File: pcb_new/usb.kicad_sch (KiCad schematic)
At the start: 28 parts, among them J14 68021-204HLF, J7 632723300011, U10 TPS2021D, U2 CAHCT1G14QDBVRQ1, U6 USB3340-EZK-TR

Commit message: initial test of new board
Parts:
- R36: Arrow ID CPF0402B8K06E1 -> (none); Description_1 CPF 0402 8K06 0.1% 25PPM 1K RL -> Thin Film Resistors - SMD 0402 8.06Kohm .1% AEC-Q200; DigiKey ID A103004CT-ND -> (none); Mfr. Name TE Connectivity -> Panasonic; Mfr. Number CPF0402B8K06E1 -> ERA-2AEB8061X; Mouser ID 279-CPF0402B8K06E1 -> 667-ERA-2AEB8061X; Mouser URL https://www.mouser.de/ProductDetail/TE-Connectivity-Holswor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 -> https://www.mouser.de/ProductDetail/Panasonic/ERA-2AEB8061X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
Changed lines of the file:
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@@
 			)
 		)
-		(property "Datasheet" "https://www.mouser.de/datasheet/2/418/8/ENG_DS_1773200_N2-1954016.pdf"
+		(property "Datasheet" "https://industrial.panasonic.com/cdbs/www-data/pdf/RDM0000/AOA0000C307.pdf"
 			(at 110.49 130.81 0)
 			(effects
@@
 			)
 		)
-		(property "Description" "CPF 0402 8K06 0.1% 25PPM 1K RL"
+		(property "Description" "Thin Film Resistors - SMD 0402 8.06Kohm .1% AEC-Q200"
 			(at 110.49 130.81 0)
 			(effects
@@
 			)
 		)
-		(property "Mouser URL" "https://www.mouser.de/ProductDetail/TE-Connectivity-Holsworthy/CPF0402B8K06E1?qs=iJVBkmKXgrk320lBsnTGsA%3D%3D&utm_source=octopart&utm_medium=aggregator&utm_campaign=279-CPF0402B8K06E1&utm_content=TE+Connectivity"
+		(property "Mouser URL" "https://www.mouser.de/ProductDetail/Panasonic/ERA-2AEB8061X?qs=nuXzIS8loXGZUdwZTdWhRQ%3D%3D"
 			(at 110.49 133.81 0)
 			(effects
@@
 			)
 		)
-		(property "Mfr. Name" "TE Connectivity"
+		(property "Mfr. Name" "Panasonic"
 			(at 110.49 133.81 0)
 			(effects
@@
 			)
 		)
-		(property "Mfr. Number" "CPF0402B8K06E1"
+		(property "Mfr. Number" "ERA-2AEB8061X"
 			(at 110.49 133.81 0)
 			(effects
@@
 			)
 		)
-		(property "DigiKey ID" "A103004CT-ND"
+		(property "DigiKey ID" ""
 			(at 110.49 133.81 0)
 			(effects
@@
 			)
 		)
-		(property "Mouser ID" "279-CPF0402B8K06E1"
+		(property "Mouser ID" "667-ERA-2AEB8061X"
 			(at 110.49 133.81 0)
 			(effects
@@
 			)
 		)
-		(property "Description_1" "CPF 0402 8K06 0.1% 25PPM 1K RL"
+		(property "Description_1" "Thin Film Resistors - SMD 0402 8.06Kohm .1% AEC-Q200"
 			(at 110.49 133.81 0)
 			(effects
@@
 			)
 		)
-		(property "Arrow ID" "CPF0402B8K06E1"
+		(property "Arrow ID" ""
 			(at 110.49 133.81 0)
 			(effects

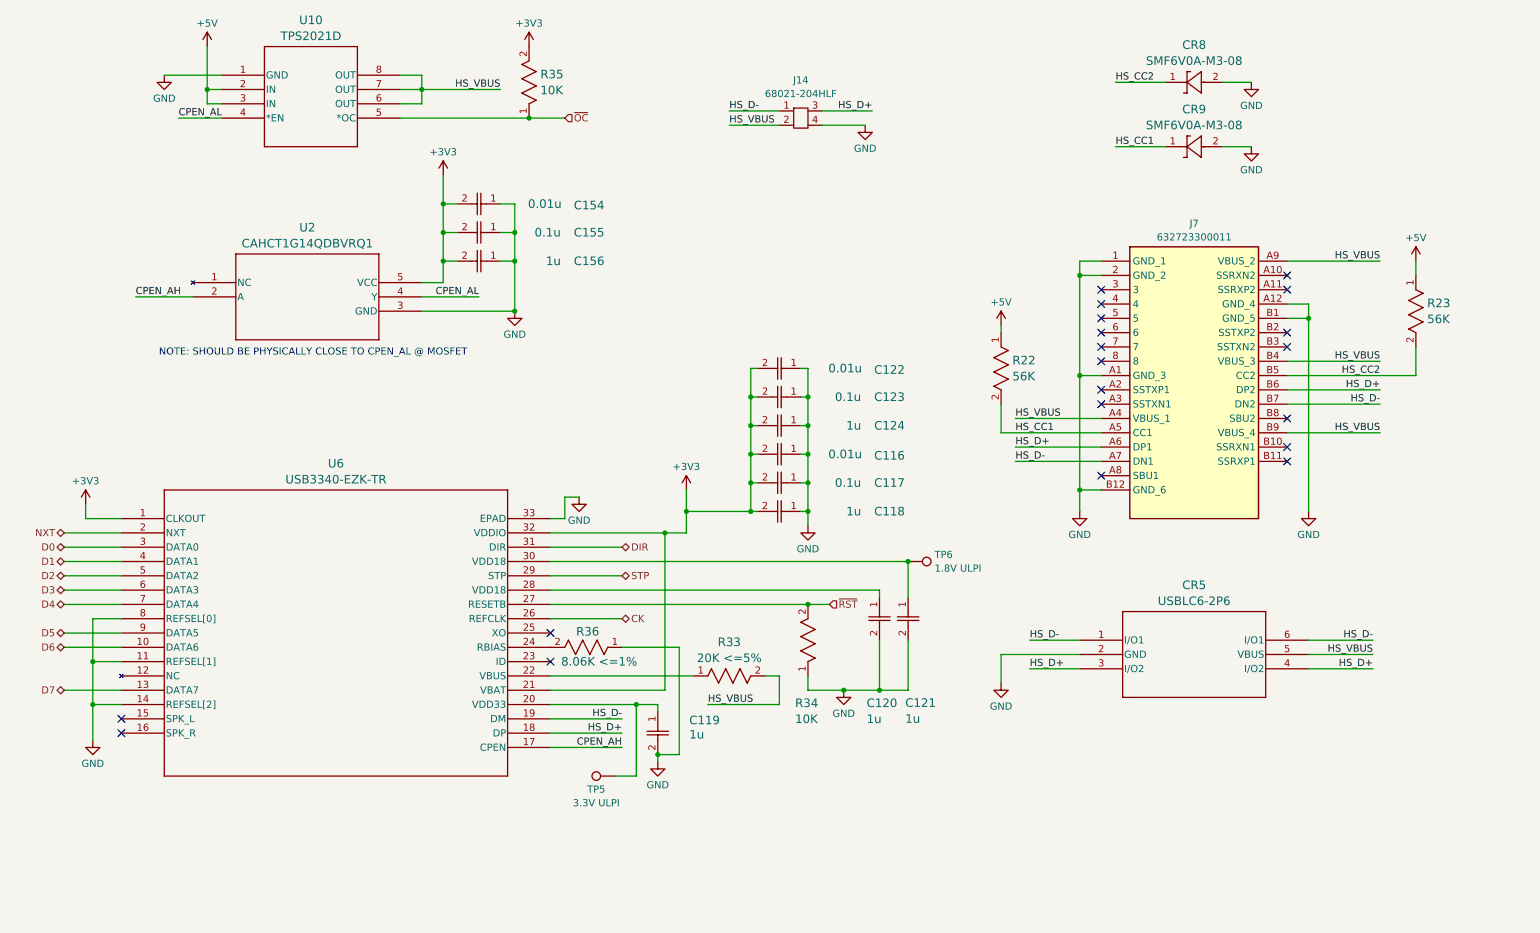
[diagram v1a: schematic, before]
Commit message: fix ULPI PHY wiring (ref #62)
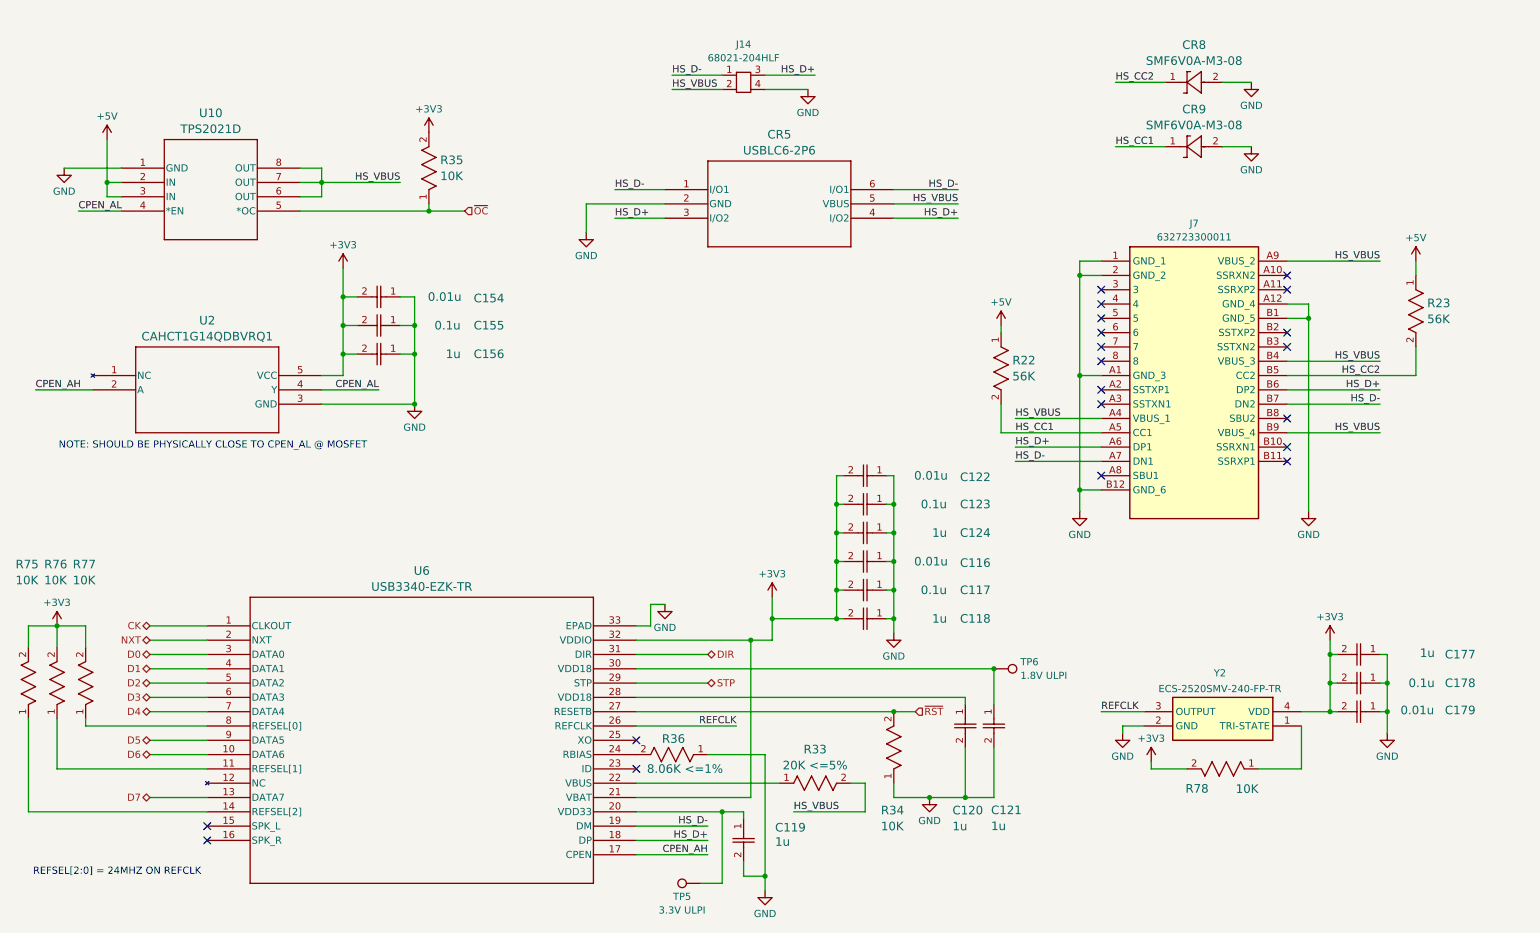
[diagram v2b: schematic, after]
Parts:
- added C177: 1u, OroLink:cap_UMK105 CG080CV-F_TAY, symbol OroLink:JMK105BJ105KVHF
- added C178: 0.1u, OroLink:CAP_MSAS1L-3_TAY, symbol OroLink:MSAST1L3YB5104KFNA01
- added C179: 0.01u, OroLink:CAP_0402_N_WAL, symbol OroLink:0402B103J160CT
- added R75, R76, R77, R78: 10K, OroLink:STA_RMCF0402_STP, symbol OroLink:RMCF0402FT10K0
- added Y2: ECS-2520SMV-240-FP-TR, ECS2520SMV240FPTR, symbol OroLink:ECS-2520SMV-240-FP-TR
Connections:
- net +3V3: now also C177.2, C178.2, C179.2, R75.2, R76.2, R77.2, R78.2, Y2.4 (VDD); no longer U6.1 (CLKOUT)
- net CK: now also U6.1 (CLKOUT); no longer U6.26 (REFCLK)
- net GND: now also C177.1, C178.1, C179.1, Y2.2 (GND); no longer U6.11 (REFSEL[1]), U6.14 (REFSEL[2]), U6.8 (REFSEL[0])
- new net: R76.1, U6.11 (REFSEL[1])
- new net: R75.1, U6.14 (REFSEL[2])
- new net: R77.1, U6.8 (REFSEL[0])
- new net: R78.1, Y2.1 (TRI-STATE)
- new net REFCLK: U6.26 (REFCLK), Y2.3 (OUTPUT)
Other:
- note added: "REFSEL[2:0] = 24MHZ ON REFCLK"
- moved on the sheet: C116, C117, C118, C119, C120, C121, C122, C123, C124, C154, C155, C156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

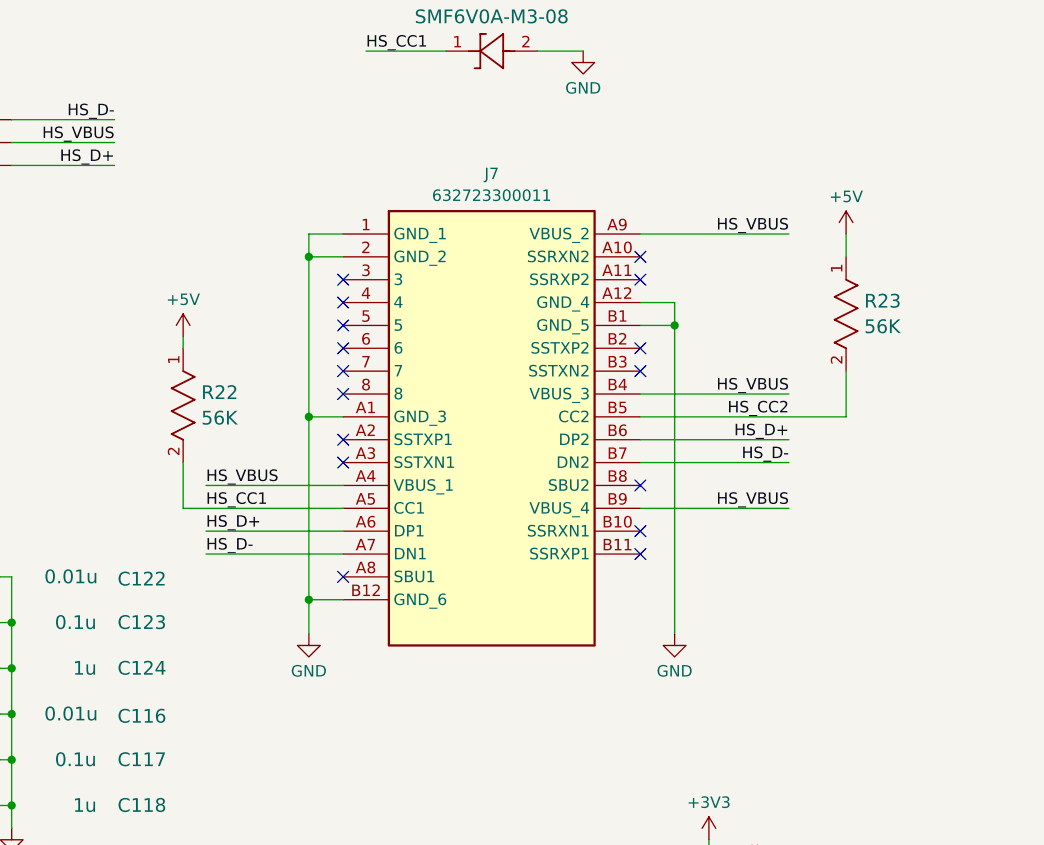
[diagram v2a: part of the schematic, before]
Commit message: replace USB-C receptacle (ref #73)
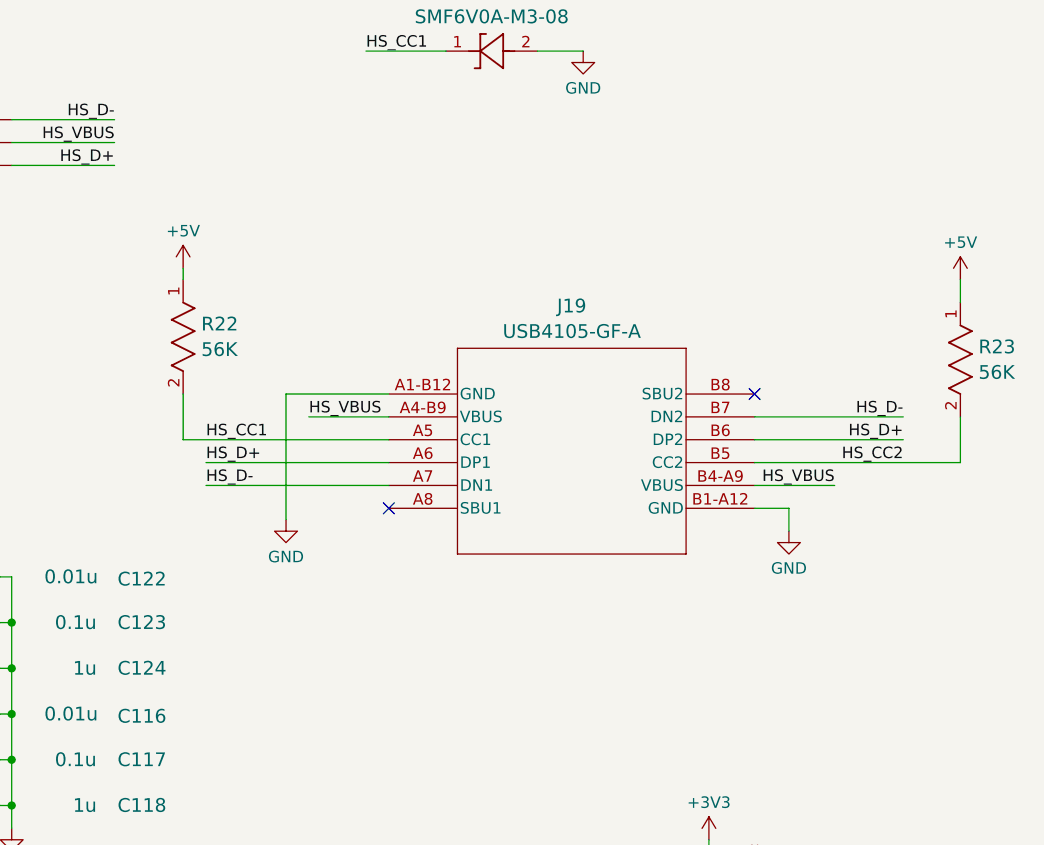
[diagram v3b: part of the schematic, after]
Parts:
- removed J7: 632723300011, OroLink:632723300011, symbol OroLink:632723300011
- added J19: USB4105-GF-A, OroLink:USB4105_GCT, symbol OroLink:USB4105-GF-A
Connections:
- net GND: now also J19.A1-B12 (GND), J19.B1-A12 (GND)
- net HS_CC1: now also J19.A5 (CC1)
- net HS_CC2: now also J19.B5 (CC2)
- net HS_D+: now also J19.A6 (DP1), J19.B6 (DP2)
- net HS_D-: now also J19.A7 (DN1), J19.B7 (DN2)
- net HS_VBUS: now also J19.A4-B9 (VBUS), J19.B4-A9 (VBUS)
- no-connect marks 20 -> 6
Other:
- moved on the sheet: R22, R23

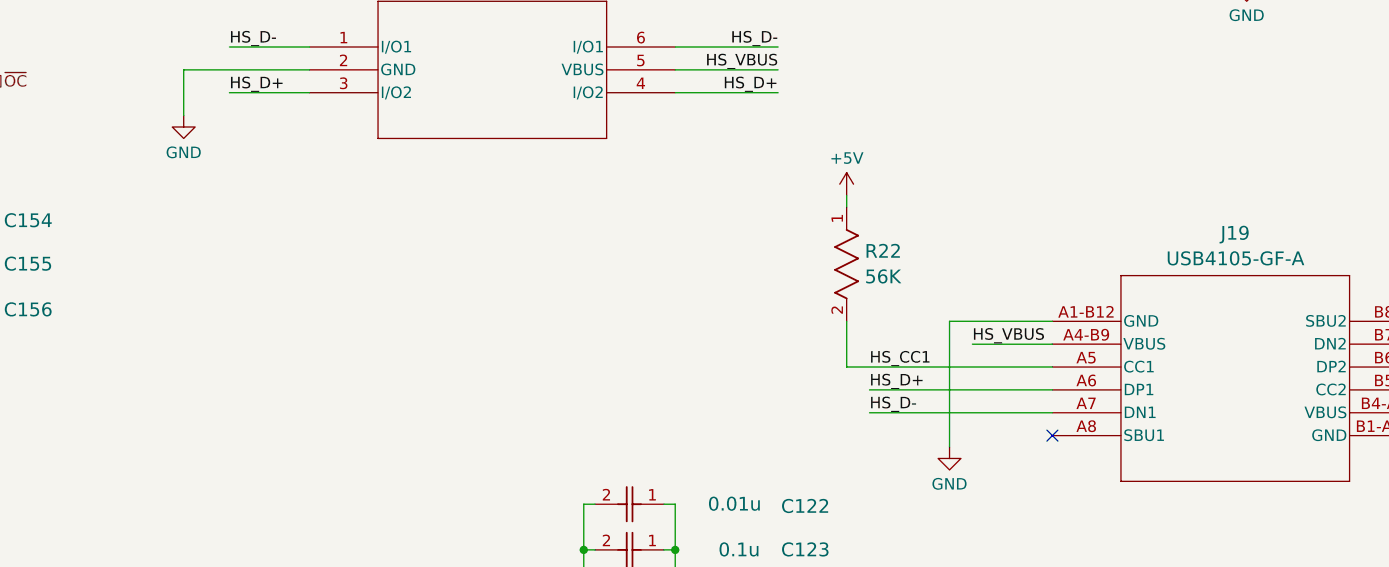
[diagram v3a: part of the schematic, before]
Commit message: mux USB rails (ref #96), adjust CC resistors (ref #87)
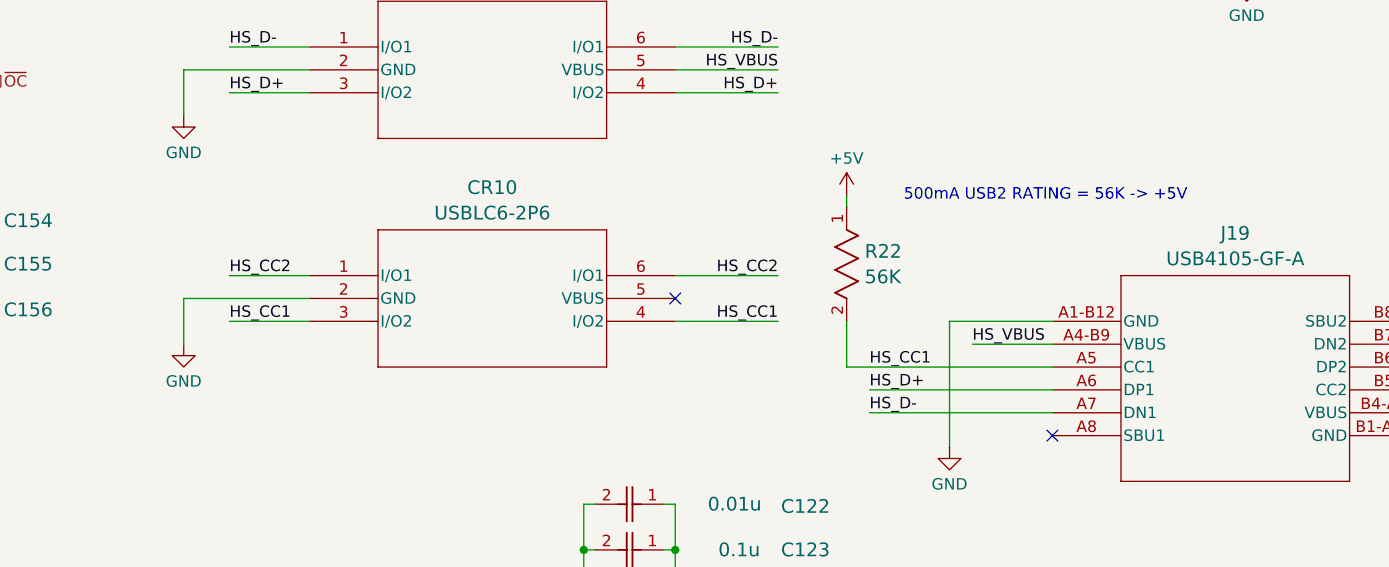
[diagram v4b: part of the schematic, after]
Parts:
- added CR10: USBLC6-2P6, OroLink:SOT-666_STM, symbol OroLink:USBLC6-2P6
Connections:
- net GND: now also CR10.2 (GND)
- net HS_CC1: now also CR10.3 (I/O2), CR10.4 (I/O2)
- net HS_CC2: now also CR10.1 (I/O1), CR10.6 (I/O1)
- no-connect marks 6 -> 7
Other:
- note added: "500mA USB2 RATING = 56K -> +5V"

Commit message: mark usb ratings (ref #87)
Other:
- note added: "VBUS RATED AT 500mA"
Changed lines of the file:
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@@
+		)
+	)
+	(text "VBUS RATED AT 500mA"
+		(exclude_from_sim no)
+		(at 69.85 32.766 0)
+		(effects
+			(font
+				(size 1.27 1.27)
+			)
 		)
 	)

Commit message: major component placement complete
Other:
- moved on the sheet: J14
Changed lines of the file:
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@@
 	(wire
 		(pts
-			(xy 132.08 31.75) (xy 140.97 31.75)
+			(xy 212.09 57.15) (xy 220.98 57.15)
 		)
 		(stroke
@@
 	(wire
 		(pts
-			(xy 156.21 31.75) (xy 148.59 31.75)
+			(xy 236.22 57.15) (xy 228.6 57.15)
 		)
 		(stroke
@@
 	(wire
 		(pts
-			(xy 140.97 29.21) (xy 132.08 29.21)
+			(xy 220.98 54.61) (xy 212.09 54.61)
 		)
 		(stroke
@@
 	(wire
 		(pts
-			(xy 148.59 29.21) (xy 157.48 29.21)
+			(xy 228.6 54.61) (xy 237.49 54.61)
 		)
 		(stroke
@@
 	)
 	(label "HS_D+"
-		(at 157.48 29.21 180)
+		(at 237.49 54.61 180)
 		(fields_autoplaced yes)
 		(effects
@@
 	)
 	(label "HS_VBUS"
-		(at 132.08 31.75 0)
+		(at 212.09 57.15 0)
 		(fields_autoplaced yes)
 		(effects
@@
 	)
 	(label "HS_D-"
-		(at 132.08 29.21 0)
+		(at 212.09 54.61 0)
 		(fields_autoplaced yes)
 		(effects
@@
 	(symbol
 		(lib_id "power:GND")
-		(at 156.21 31.75 0)
+		(at 236.22 57.15 0)
 		(unit 1)
 		(exclude_from_sim no)
@@
 		(fields_autoplaced yes)
 		(property "Reference" "#PWR0110"
-			(at 156.21 38.1 0)
+			(at 236.22 63.5 0)
 			(effects
 				(font
@@
 		)
 		(property "Value" "GND"
-			(at 156.21 35.8831 0)
+			(at 236.22 61.2831 0)
 			(effects
 				(font
@@
 		)
 		(property "Footprint" ""
-			(at 156.21 31.75 0)
+			(at 236.22 57.15 0)
 			(effects
 				(font
@@
 		)
 		(property "Datasheet" ""
-			(at 156.21 31.75 0)
+			(at 236.22 57.15 0)
 			(effects
 				(font
@@
 		)
 		(property "Description" "Power symbol creates a global label with name \"GND\" , ground"
-			(at 156.21 31.75 0)
+			(at 236.22 57.15 0)
 			(effects
 				(font
@@
 	(symbol
 		(lib_id "OroLink:68021-204HLF")
-		(at 140.97 26.67 0)
+		(at 220.98 52.07 0)
 		(unit 1)
 		(exclude_from_sim no)
@@
 		(dnp no)
 		(property "Reference" "J14"
-			(at 144.78 23.7377 0)
+			(at 224.79 49.1377 0)
 			(effects
 				(font
@@
 		)
 		(property "Value" "68021-204HLF"
-			(at 144.78 26.162 0)
+			(at 224.79 51.562 0)
 			(effects
 				(font
@@
 		)
 		(property "Footprint" "OroLink:2x2 4p 2.54 pitch"
-			(at 140.97 26.67 0)
+			(at 220.98 52.07 0)
 			(effects
 				(font
@@
 		)
 		(property "Datasheet" "https://cdn.amphenol-cs.com/media/wysiwyg/files/documentation/datasheet/boardwiretoboard/bwb_bergstik.pdf"
-			(at 140.97 26.67 0)
+			(at 220.98 52.07 0)
 			(effects
 				(font
@@
 		)
 		(property "Description" " Headers & Wire Housings 4P SR UNSHRD HRD .38 GOLD OVER NI"
-			(at 140.97 26.67 0)
+			(at 220.98 52.07 0)
 			(effects
 				(font
@@
 		)
 		(property "Mouser ID Number" "649-68021-204HLF"
-			(at 140.97 26.67 0)
+			(at 220.98 52.07 0)
 			(effects
 				(font
@@
 		)
 		(property "Mouser Stock URL" "https://www.mouser.de/ProductDetail/Amphenol-FCI/68021-204HLF?qs=QKvFUfBIyQLYRGZzFGyTzg%3D%3D"
-			(at 140.97 26.67 0)
+			(at 220.98 52.07 0)
 			(effects
 				(font
@@
 		(on_board yes)
 		(dnp no)
-		(fields_autoplaced yes)
 		(property "Reference" "CR10"
 			(at 151.13 65.1561 0)
